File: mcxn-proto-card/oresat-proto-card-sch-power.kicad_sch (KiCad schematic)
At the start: 87 parts, among them Q1 DMP2110UVTQ-7, Q2 DMPH2040UVTQ-7, Q7 DMPH2040UVTQ-7, Q8 DMN2050LQ-7, Q9 DMN2050LQ-7, U10 TPS62111RSA, U11 MIC842LYC5, U12 MIC842LYC5, U2 MAX7310, U3 TS5A21366DCUR, U6 MAX4211FETE

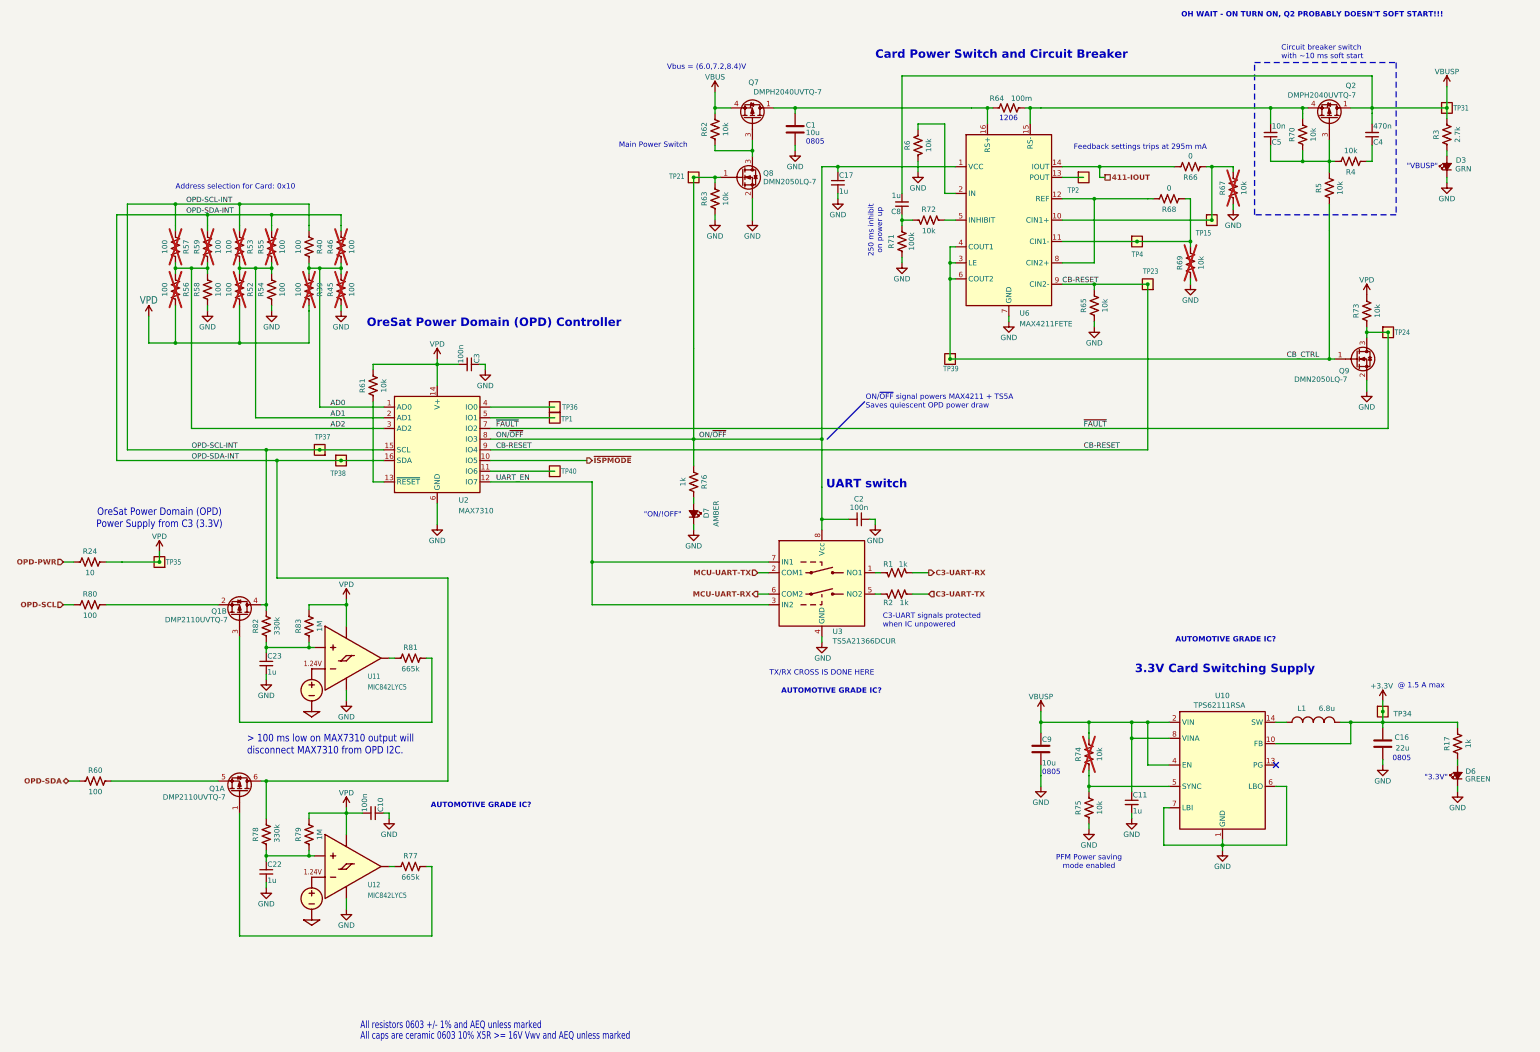
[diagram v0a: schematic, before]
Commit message: Updated BOM to match OPD writeup; Best Possible OPD now? Maybe?
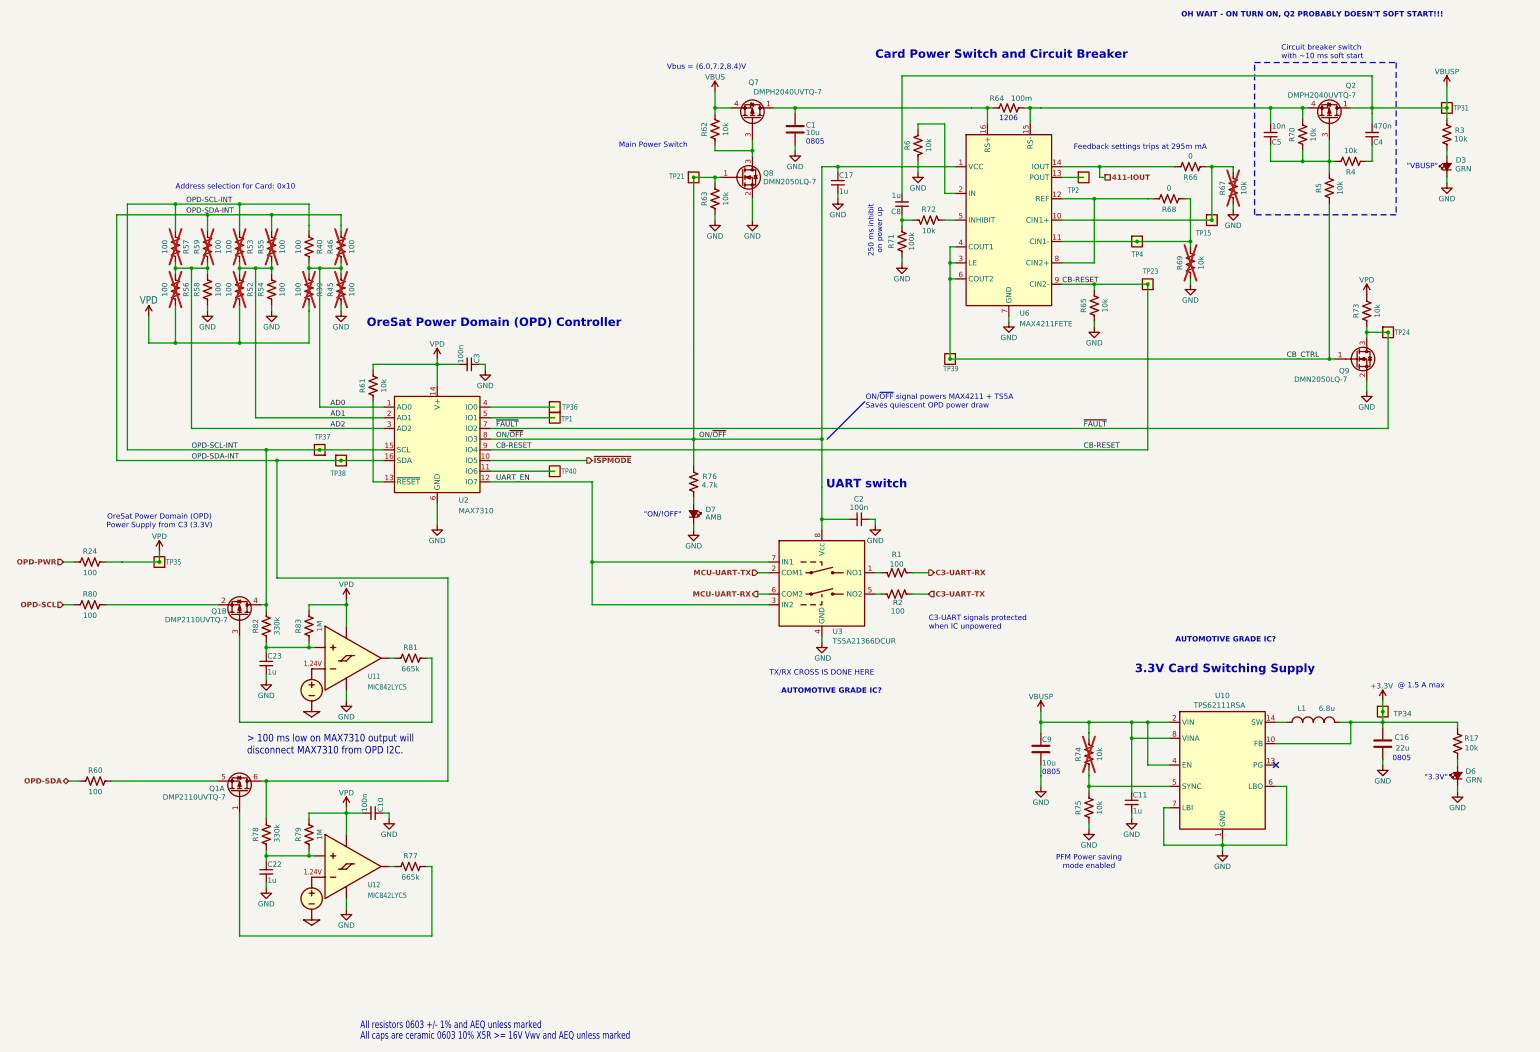
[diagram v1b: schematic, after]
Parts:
- D6: value GREEN -> GRN
- D7: value AMBER -> AMB
- R1, R2: value 1k -> 100; DPN RMCF0603FT1K00CT-ND -> RMCF0603FT100RCT-ND; MPN RMCF0603FT1K00 -> RMCF0603FT100R
- R17: value 1k -> 10k; DPN RMCF0603FT1K00CT-ND -> RMCF0603FT10K0CT-ND; MPN RMCF0603FT1K00 -> RMCF0603FT10K0
- R24: value 10 -> 100; DPN RMCF0603FT10R0CT-ND -> RMCF0603FT100RCT-ND; MPN RMCF0603FT10R0 -> RMCF0603FT100R
- R3: value 2.7k -> 10k; DPN RMCF0603FT2K70CT-ND -> RMCF0603FT10K0CT-ND; MPN RMCF0603FT2K70 -> RMCF0603FT10K0
- R76: value 1k -> 4.7k; DPN RMCF0603FT1K00CT-ND -> RMCF0603FT4K70CT-ND; MPN RMCF0603FT1K00 -> RMCF0603FT4K70
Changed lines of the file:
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@@
 	(text "C3-UART signals protected\nwhen IC unpowered"
 		(exclude_from_sim no)
-		(at 237.998 164.592 0)
+		(at 248.92 165.1 0)
 		(effects
 			(font
@@
 		(effects
 			(font
-				(size 1.778 1.5113)
+				(size 1.27 1.27)
 			)
 			(justify bottom)
@@
 		)
 	)
-	(text "AUTOMOTIVE GRADE IC?\n"
-		(exclude_from_sim no)
-		(at 142.494 210.312 0)
-		(effects
-			(font
-				(size 1.27 1.27)
-				(thickness 0.254)
-				(bold yes)
-				(color 255 0 0 1)
-			)
-		)
-	)
 	(text "\"VBUSP\""
 		(exclude_from_sim no)
@@
 		(dnp no)
 		(property "Reference" "R3"
-			(at 369.57 50.8 90)
+			(at 375.158 49.784 0)
 			(show_name no)
 			(do_not_autoplace no)
@@
 			)
 		)
-		(property "Value" "2.7k"
-			(at 374.65 50.8 90)
+		(property "Value" "10k"
+			(at 375.412 51.816 0)
 			(show_name no)
 			(do_not_autoplace no)
@@
 			)
 		)
-		(property "Description" "2.7 kOhms ±1% 0.1W, 1/10W Chip Resistor 0603 (1608 Metric) Automotive AEC-Q200 Thick Film"
+		(property "Description" "10 kOhms ±1% 0.1W, 1/10W Chip Resistor 0603 (1608 Metric) Automotive AEC-Q200 Thick Film"
 			(at 372.11 50.8 0)
 			(hide yes)
@@
 			)
 		)
-		(property "DPN" "RMCF0603FT2K70CT-ND"
+		(property "DPN" "RMCF0603FT10K0CT-ND"
 			(at 372.11 50.8 0)
 			(hide yes)
@@
 			)
 		)
-		(property "MPN" "RMCF0603FT2K70"
+		(property "MPN" "RMCF0603FT10K0"
 			(at 372.11 50.8 0)
 			(hide yes)
@@
 		(dnp no)
 		(property "Reference" "D7"
-			(at 195.326 141.986 0)
+			(at 195.834 139.192 90)
 			(show_name no)
 			(do_not_autoplace no)
@@
 			)
 		)
-		(property "Value" "AMBER"
-			(at 199.136 144.018 0)
+		(property "Value" "AMB"
+			(at 195.834 142.494 90)
 			(show_name no)
 			(do_not_autoplace no)
@@
 			)
 		)
-		(property "Value" "10"
+		(property "Value" "100"
 			(at 49.53 154.94 90)
 			(show_name no)
@@
 			)
 		)
-		(property "Description" "10 Ohms ±1% 0.1W, 1/10W Chip Resistor 0603 (1608 Metric) Automotive AEC-Q200 Thick Film"
+		(property "Description" "100 Ohms ±1% 0.1W, 1/10W Chip Resistor 0603 (1608 Metric) Automotive AEC-Q200 Thick Film"
 			(at 49.53 152.4 0)
 			(hide yes)
@@
 			)
 		)
-		(property "DPN" "RMCF0603FT10R0CT-ND"
+		(property "DPN" "RMCF0603FT100RCT-ND"
 			(at 49.53 152.4 0)
 			(hide yes)
@@
 			)
 		)
-		(property "MPN" "RMCF0603FT10R0"
+		(property "MPN" "RMCF0603FT100R"
 			(at 49.53 152.4 0)
 			(hide yes)
@@
 		(dnp no)
 		(property "Reference" "R1"
-			(at 239.268 152.908 90)
+			(at 241.3 150.622 90)
 			(show_name no)
 			(do_not_autoplace no)
@@
 			)
 		)
-		(property "Value" "1k"
-			(at 242.824 152.908 90)
+		(property "Value" "100"
+			(at 241.3 152.908 90)
 			(show_name no)
 			(do_not_autoplace no)
@@
 			)
 		)
-		(property "Description" "1 kOhms ±1% 0.1W, 1/10W Chip Resistor 0603 (1608 Metric) Automotive AEC-Q200 Thick Film"
+		(property "Description" "100 Ohms ±1% 0.1W, 1/10W Chip Resistor 0603 (1608 Metric) Automotive AEC-Q200 Thick Film"
 			(at 241.3 154.94 0)
 			(hide yes)
@@
 			)
 		)
-		(property "DPN" "RMCF0603FT1K00CT-ND"
+		(property "DPN" "RMCF0603FT100RCT-ND"
 			(at 241.3 154.94 90)
 			(hide yes)
@@
 			)
 		)
-		(property "MPN" "RMCF0603FT1K00"
+		(property "MPN" "RMCF0603FT100R"
 			(at 241.3 154.94 90)
 			(hide yes)
@@
 		(dnp no)
 		(property "Reference" "R76"
-			(at 195.58 133.35 90)
+			(at 196.85 132.08 0)
 			(show_name no)
 			(do_not_autoplace no)
@@
 			)
 		)
-		(property "Value" "1k"
-			(at 190.5 133.35 90)
+		(property "Value" "4.7k"
+			(at 196.85 134.112 0)
 			(show_name no)
 			(do_not_autoplace no)
@@
 			)
 		)
-		(property "Description" "1 kOhms ±1% 0.1W, 1/10W Chip Resistor 0603 (1608 Metric) Automotive AEC-Q200 Thick Film"
+		(property "Description" "4.7 kOhms ±1% 0.1W, 1/10W Chip Resistor 0603 (1608 Metric) Automotive AEC-Q200 Thick Film"
 			(at 193.04 133.35 0)
 			(hide yes)
@@
 			)
 		)
-		(property "DPN" "RMCF0603FT1K00CT-ND"
+		(property "DPN" "RMCF0603FT4K70CT-ND"
 			(at 193.04 133.35 0)
 			(hide yes)
@@
 			)
 		)
-		(property "MPN" "RMCF0603FT1K00"
+		(property "MPN" "RMCF0603FT4K70"
 			(at 193.04 133.35 0)
 			(hide yes)
@@
 			)
 		)
-		(property "Value" "GREEN"
-			(at 382.524 204.724 90)
+		(property "Value" "GRN"
+			(at 380.492 204.978 90)
 			(show_name no)
 			(do_not_autoplace no)
@@
 		(dnp no)
 		(property "Reference" "R17"
-			(at 372.11 195.58 90)
+			(at 377.952 194.31 0)
 			(show_name no)
 			(do_not_autoplace no)
@@
 			)
 		)
-		(property "Value" "1k"
-			(at 377.19 195.58 90)
+		(property "Value" "10k"
+			(at 377.952 196.596 0)
 			(show_name no)
 			(do_not_autoplace no)
@@
 			)
 		)
-		(property "Description" "1 kOhms ±1% 0.1W, 1/10W Chip Resistor 0603 (1608 Metric) Automotive AEC-Q200 Thick Film"
+		(property "Description" "10 kOhms ±1% 0.1W, 1/10W Chip Resistor 0603 (1608 Metric) Automotive AEC-Q200 Thick Film"
 			(at 374.65 195.58 0)
 			(hide yes)
@@
 			)
 		)
-		(property "DPN" "RMCF0603FT1K00CT-ND"
+		(property "DPN" "RMCF0603FT10K0CT-ND"
 			(at 374.65 195.58 0)
 			(hide yes)
@@
 			)
 		)
-		(property "MPN" "RMCF0603FT1K00"
+		(property "MPN" "RMCF0603FT10K0"
 			(at 374.65 195.58 0)
 			(hide yes)
@@
 		(dnp no)
 		(property "Reference" "R2"
-			(at 239.268 162.052 90)
+			(at 241.554 162.052 90)
 			(show_name no)
 			(do_not_autoplace no)
@@
 			)
 		)
-		(property "Value" "1k"
-			(at 243.078 162.052 90)
+		(property "Value" "100"
+			(at 241.554 164.084 90)
 			(show_name no)
 			(do_not_autoplace no)
@@
 			)
 		)
-		(property "Description" "1 kOhms ±1% 0.1W, 1/10W Chip Resistor 0603 (1608 Metric) Automotive AEC-Q200 Thick Film"
+		(property "Description" "100 Ohms ±1% 0.1W, 1/10W Chip Resistor 0603 (1608 Metric) Automotive AEC-Q200 Thick Film"
 			(at 241.3 160.02 0)
 			(hide yes)
@@
 			)
 		)
-		(property "DPN" "RMCF0603FT1K00CT-ND"
+		(property "DPN" "RMCF0603FT100RCT-ND"
 			(at 241.3 160.02 90)
 			(hide yes)
@@
 			)
 		)
-		(property "MPN" "RMCF0603FT1K00"
+		(property "MPN" "RMCF0603FT100R"
 			(at 241.3 160.02 90)
 			(hide yes)

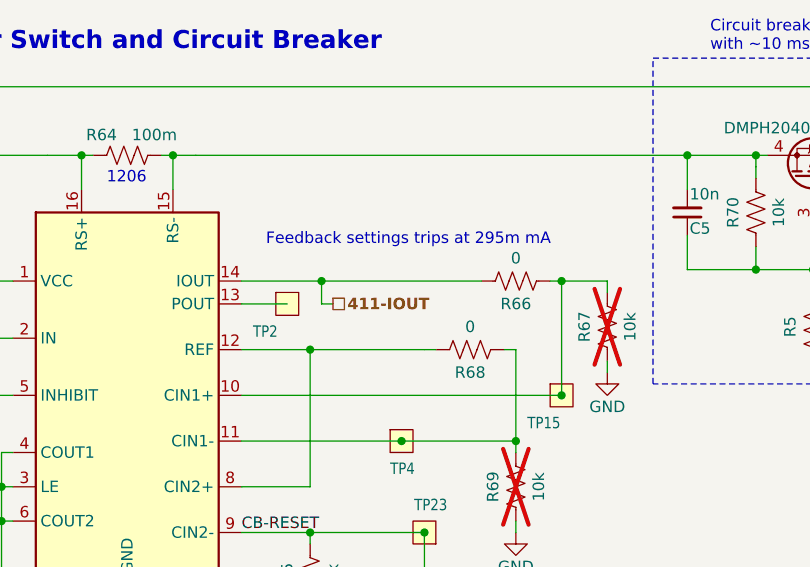
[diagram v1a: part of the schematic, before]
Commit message: Saved a zero ohm by replacing it with a 100 ohms
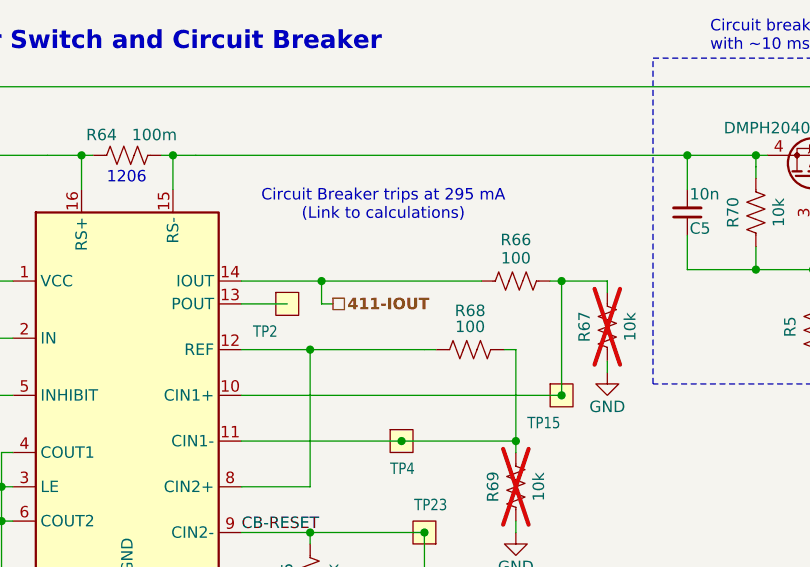
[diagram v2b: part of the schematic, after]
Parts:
- R66, R68: value 0 -> 100; DPN RMCF0603ZT0R00CT-ND -> RMCF0603FT100RCT-ND; MPN RMCF0603ZT0R00 -> RMCF0603FT100R
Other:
- note added: "Circuit Breaker trips at 295 mA (Link to calculations)"
- note removed: "Feedback settings trips at 295m mA"
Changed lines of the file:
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@@
 		)
 	)
-	(text "Feedback settings trips at 295m mA"
+	(text "Circuit Breaker trips at 295 mA\n(Link to calculations)"
 		(exclude_from_sim no)
-		(at 299.212 53.848 0)
+		(at 296.418 50.038 0)
 		(effects
 			(font
 				(size 1.27 1.27)
 			)
+			(href "https://docs.google.com/spreadsheets/d/1PE7U5m56bN0CZ0h20G8QKrn_dD4fJunBUuOQCO6Czg8/edit?usp=sharing")
 		)
 	)
@@
 		(dnp no)
 		(property "Reference" "R68"
-			(at 306.07 68.58 90)
+			(at 306.07 61.722 90)
 			(show_name no)
 			(do_not_autoplace no)
@@
 			)
 		)
-		(property "Value" "0"
+		(property "Value" "100"
 			(at 306.07 63.5 90)
 			(show_name no)
@@
 			)
 		)
-		(property "Description" "0 Ohms Jumper Chip Resistor 0603 (1608 Metric) Automotive AEC-Q200 Thick Film"
+		(property "Description" "100 Ohms ±1% 0.1W, 1/10W Chip Resistor 0603 (1608 Metric) Automotive AEC-Q200 Thick Film"
 			(at 306.07 66.04 0)
 			(hide yes)
@@
 			)
 		)
-		(property "DPN" "RMCF0603ZT0R00CT-ND"
+		(property "DPN" "RMCF0603FT100RCT-ND"
 			(at 306.07 66.04 0)
 			(hide yes)
@@
 			)
 		)
-		(property "MPN" "RMCF0603ZT0R00"
+		(property "MPN" "RMCF0603FT100R"
 			(at 306.07 66.04 0)
 			(hide yes)
@@
 		(dnp no)
 		(property "Reference" "R66"
-			(at 311.15 60.96 90)
+			(at 311.15 53.848 90)
 			(show_name no)
 			(do_not_autoplace no)
@@
 			)
 		)
-		(property "Value" "0"
+		(property "Value" "100"
 			(at 311.15 55.88 90)
 			(show_name no)
@@
 			)
 		)
-		(property "Description" "0 Ohms Jumper Chip Resistor 0603 (1608 Metric) Automotive AEC-Q200 Thick Film"
+		(property "Description" "100 Ohms ±1% 0.1W, 1/10W Chip Resistor 0603 (1608 Metric) Automotive AEC-Q200 Thick Film"
 			(at 311.15 58.42 0)
 			(hide yes)
@@
 			)
 		)
-		(property "DPN" "RMCF0603ZT0R00CT-ND"
+		(property "DPN" "RMCF0603FT100RCT-ND"
 			(at 311.15 58.42 0)
 			(hide yes)
@@
 			)
 		)
-		(property "MPN" "RMCF0603ZT0R00"
+		(property "MPN" "RMCF0603FT100R"
 			(at 311.15 58.42 0)
 			(hide yes)

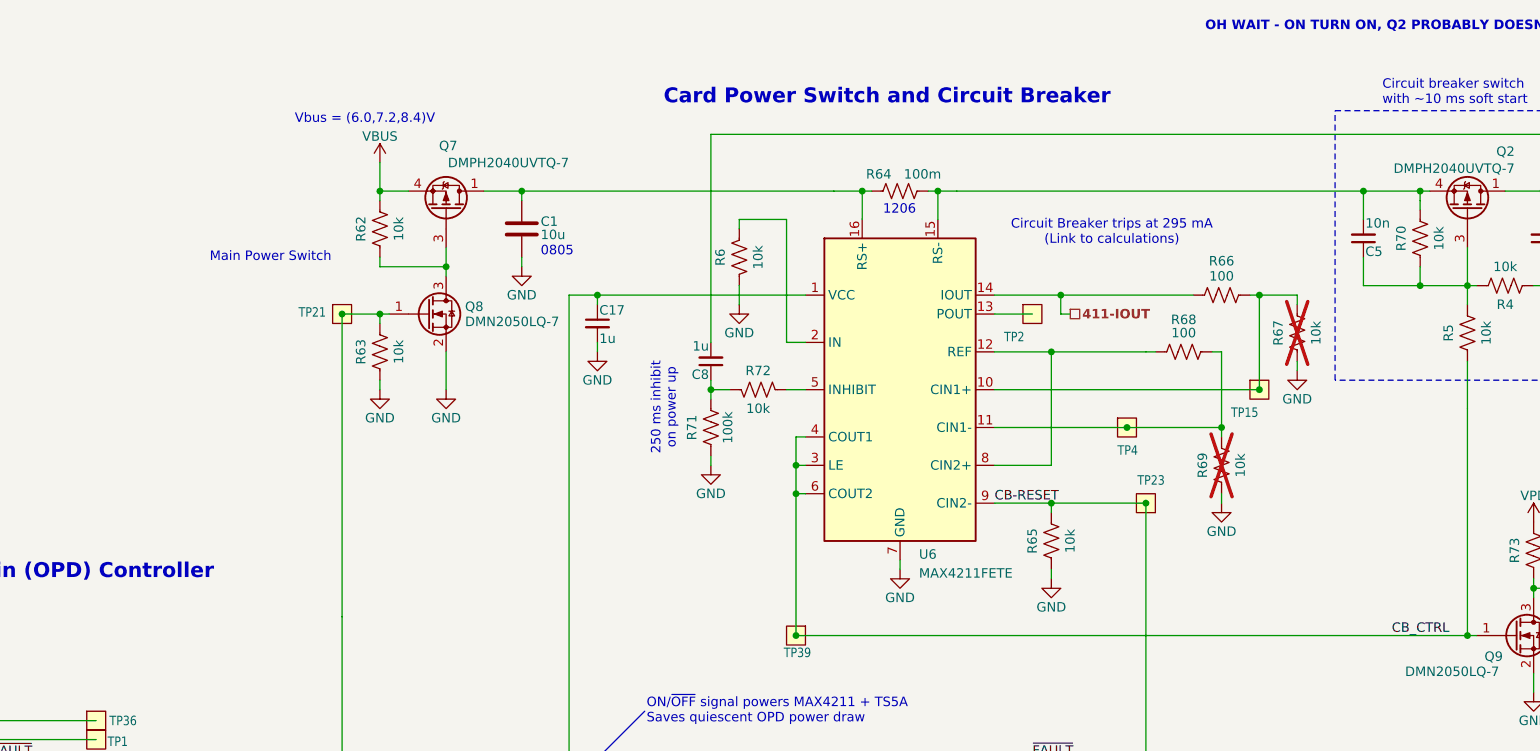
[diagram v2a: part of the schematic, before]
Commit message: OPD Fix
TCAN change from 330 to 337, added ISP TP, made PO_23:21 the version pins, added capacitor and resistor for OPD fix, and changed revision to 6.2
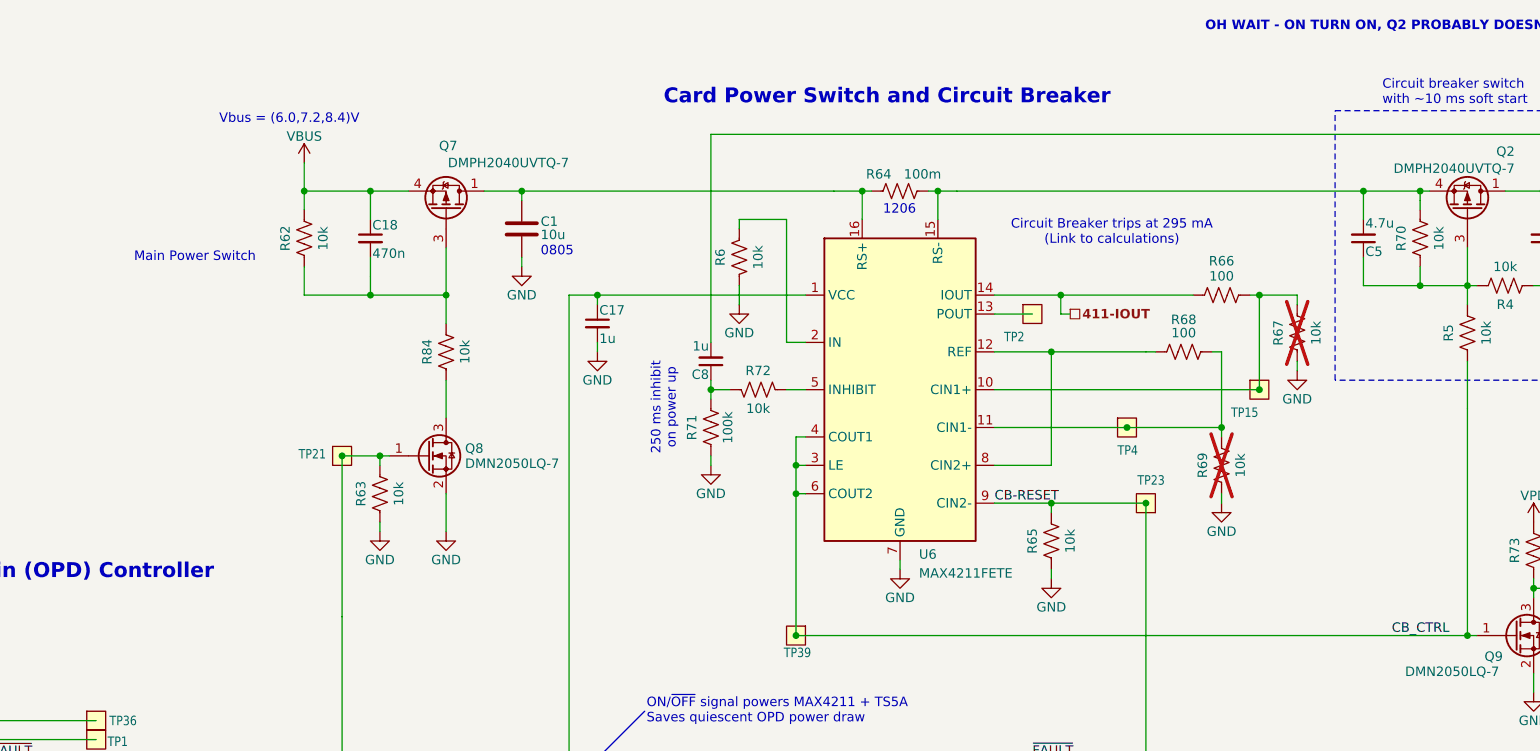
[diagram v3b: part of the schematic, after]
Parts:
- added C18: 470n, oresat-passives:0603-C-NOSILK, symbol Device:C_Small
- added R84: 10k, oresat-passives:0603-C-NOSILK, symbol Device:R_US
- C5: value 10n -> 4.7u
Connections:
- net VBUS: now also C18.1
- net at Q7.3 (G), R62.1: now also C18.2, R84.2; no longer Q8.3 (D)
- new net: Q8.3 (D), R84.1
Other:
- moved on the sheet: Q8, R62, R63, TP21
